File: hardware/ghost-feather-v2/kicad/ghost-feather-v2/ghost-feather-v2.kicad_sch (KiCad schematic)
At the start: 21 parts, among them J1 Conn_ARM_SWD_TagConnect_TC203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, SW1 BOOT0, U1 STM32F722RETx, U2 BMI088

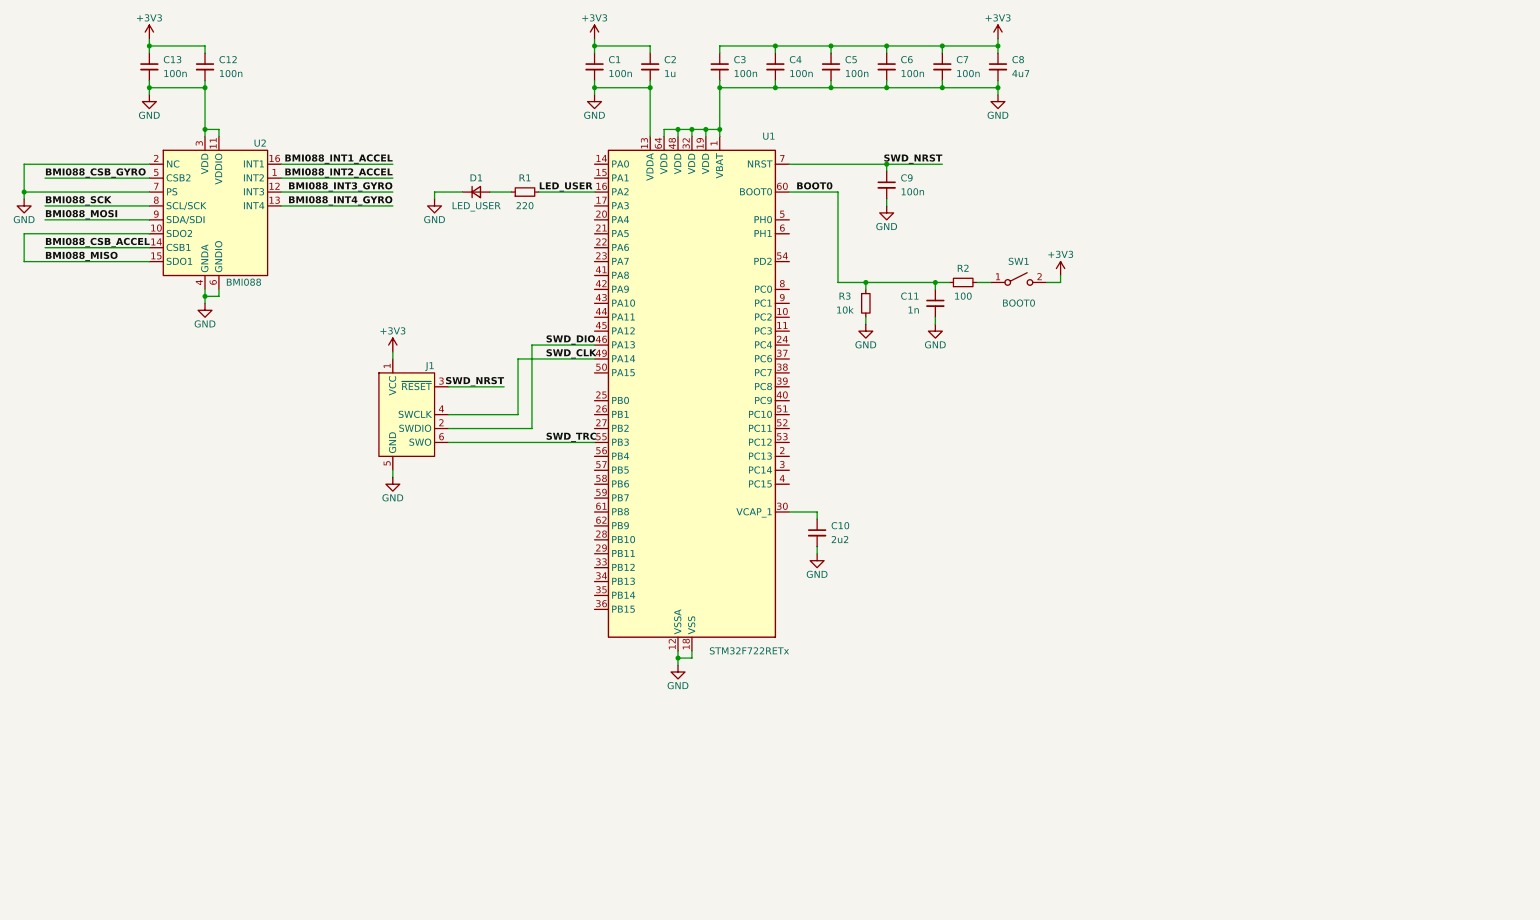
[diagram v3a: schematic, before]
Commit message: feat: hardware: Add ghost-feather-v2 IIS2MDCTR sensor
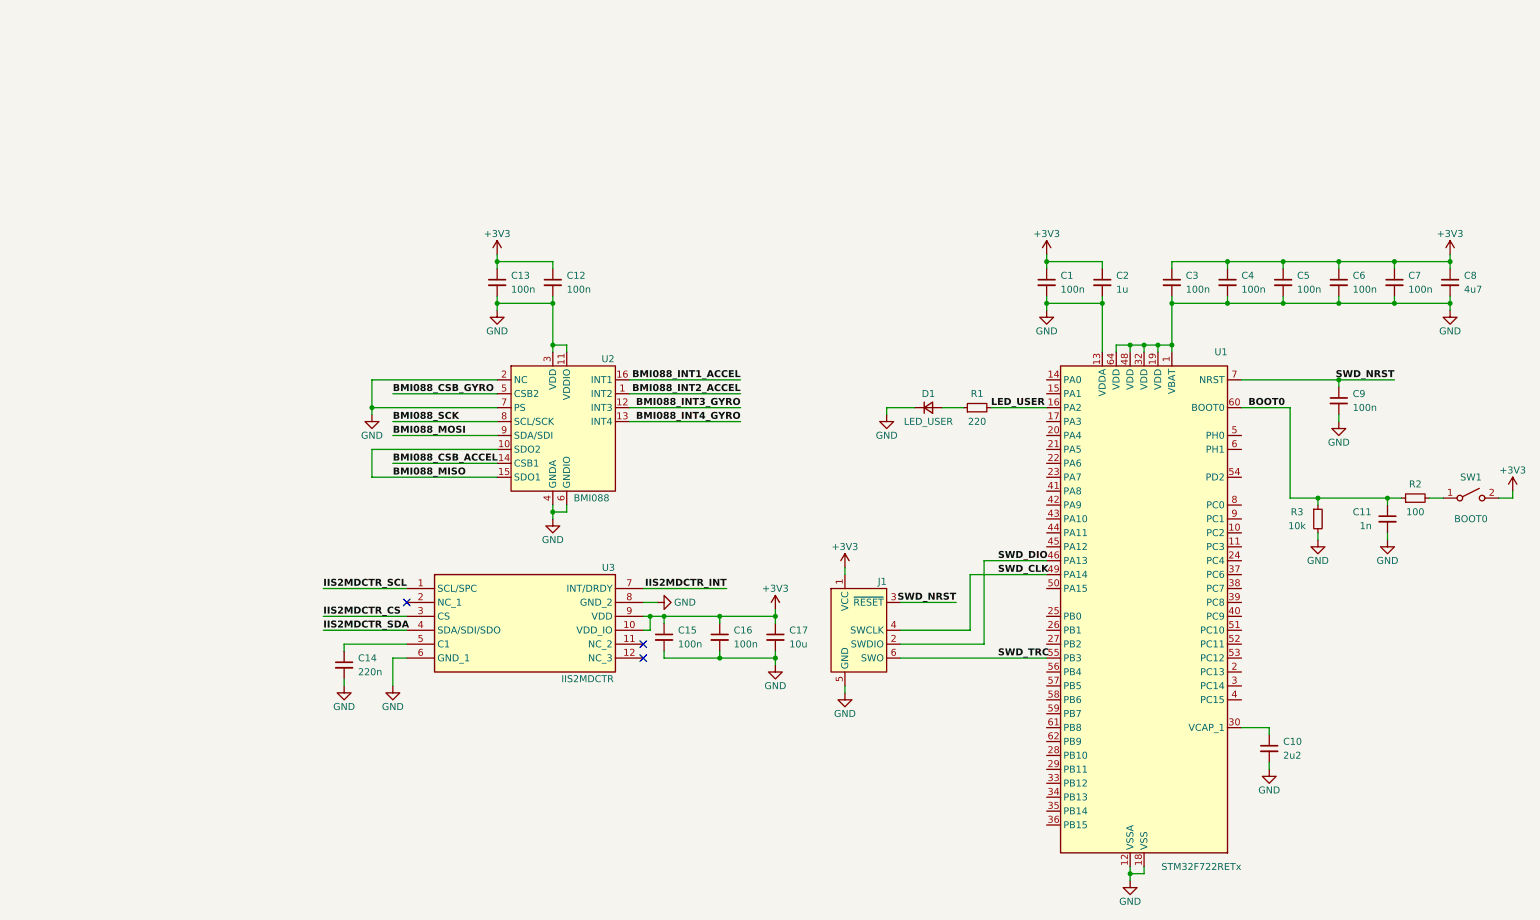
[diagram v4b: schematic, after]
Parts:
- added C14: 220n, symbol Device:C_Small
- added C15, C16: 100n, symbol Device:C_Small
- added C17: 10u, symbol Device:C_Small
- added U3: IIS2MDCTR, IIS2MDCTR, symbol IIS2MDCTR:IIS2MDCTR
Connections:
- net +3V3: now also C15.1, C16.1, C17.1, U3.10 (VDD_IO), U3.9 (VDD)
- net GND: now also C14.2, C15.2, C16.2, C17.2, U3.6 (GND_1), U3.8 (GND_2)
- new net: C14.1, U3.5 (C1)
- new net IIS2MDCTR_CS: U3.3 (CS)
- new net IIS2MDCTR_INT: U3.7 (INT/DRDY)
- new net IIS2MDCTR_SCL: U3.1 (SCL/SPC)
- new net IIS2MDCTR_SDA: U3.4 (SDA/SDI/SDO)
- no-connect marks 0 -> 3
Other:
- moved on the sheet: C1, C10, C11, C12, C13, C2, C3, C4, C5, C6, C7, C8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

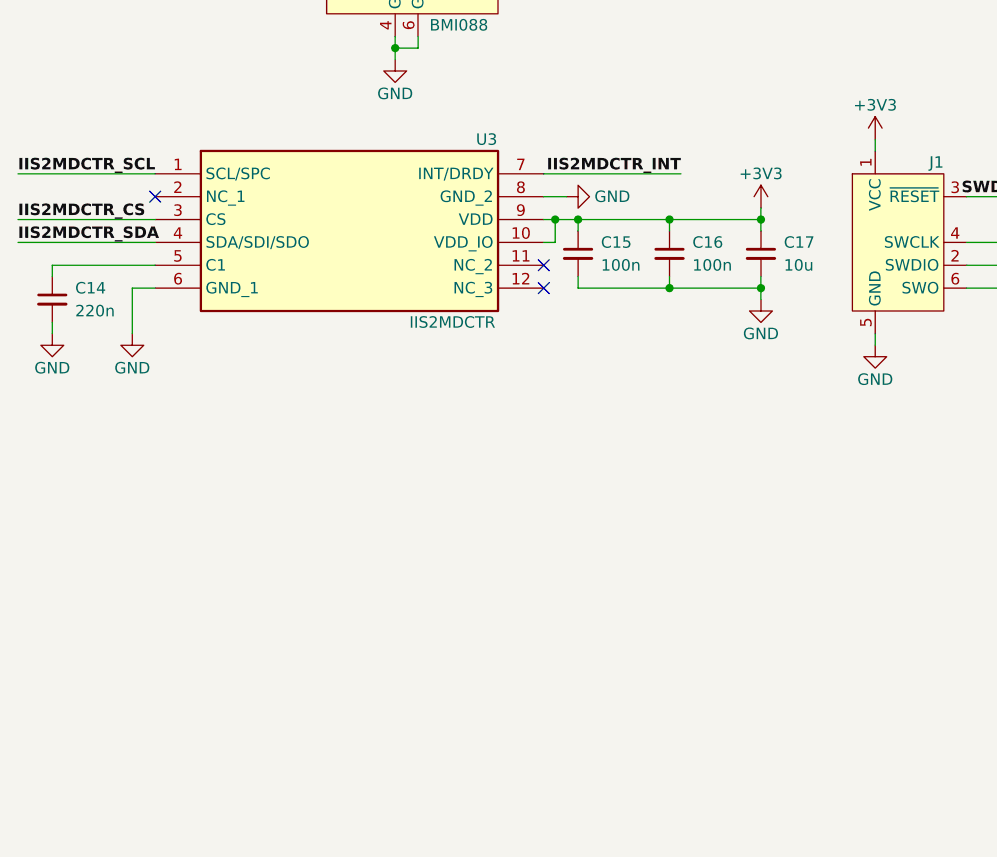
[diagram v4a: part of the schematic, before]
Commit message: feat: hardware: Add ghost-feather-v2 BMP390 sensor
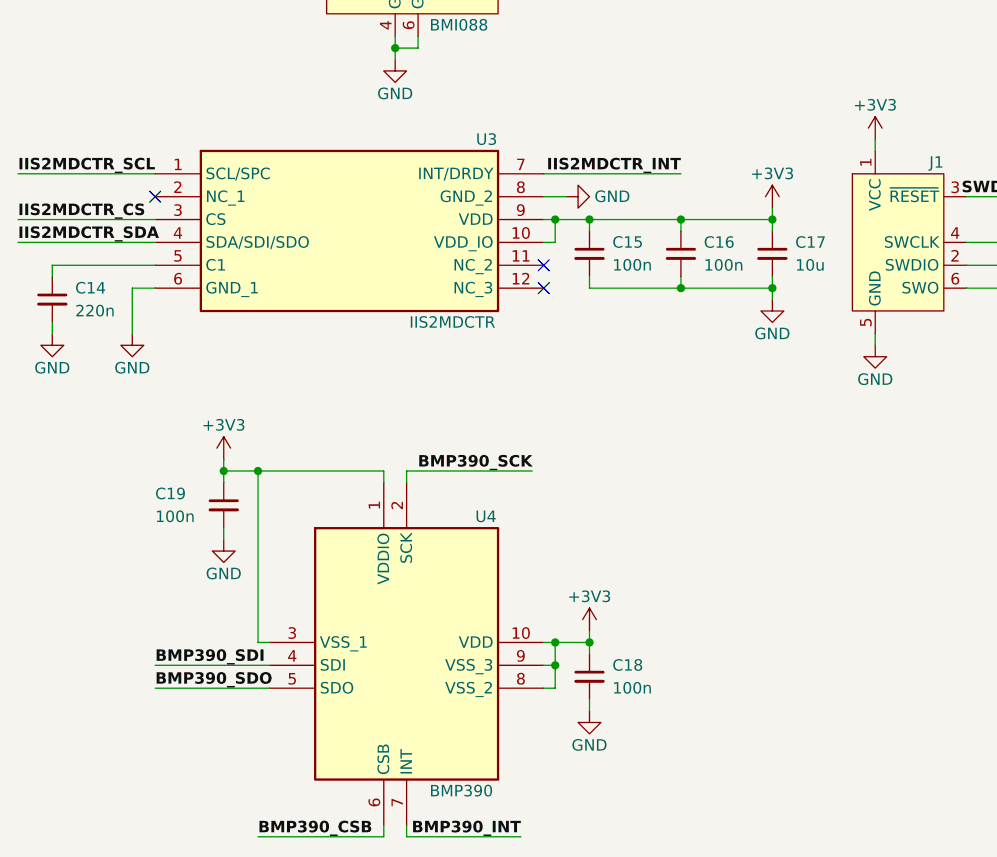
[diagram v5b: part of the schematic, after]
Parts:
- added C18, C19: 100n, symbol Device:C_Small
- added U4: BMP390, BMP390, symbol BMP390:BMP390
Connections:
- net +3V3: now also C18.1, C19.1, U4.1 (VDDIO), U4.10 (VDD), U4.3 (VSS_1), U4.8 (VSS_2), U4.9 (VSS_3)
- net GND: now also C18.2, C19.2
- new net BMP390_CSB: U4.6 (CSB)
- new net BMP390_INT: U4.7 (INT)
- new net BMP390_SCK: U4.2 (SCK)
- new net BMP390_SDI: U4.4 (SDI)
- new net BMP390_SDO: U4.5 (SDO)
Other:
- moved on the sheet: C15, C16, C17

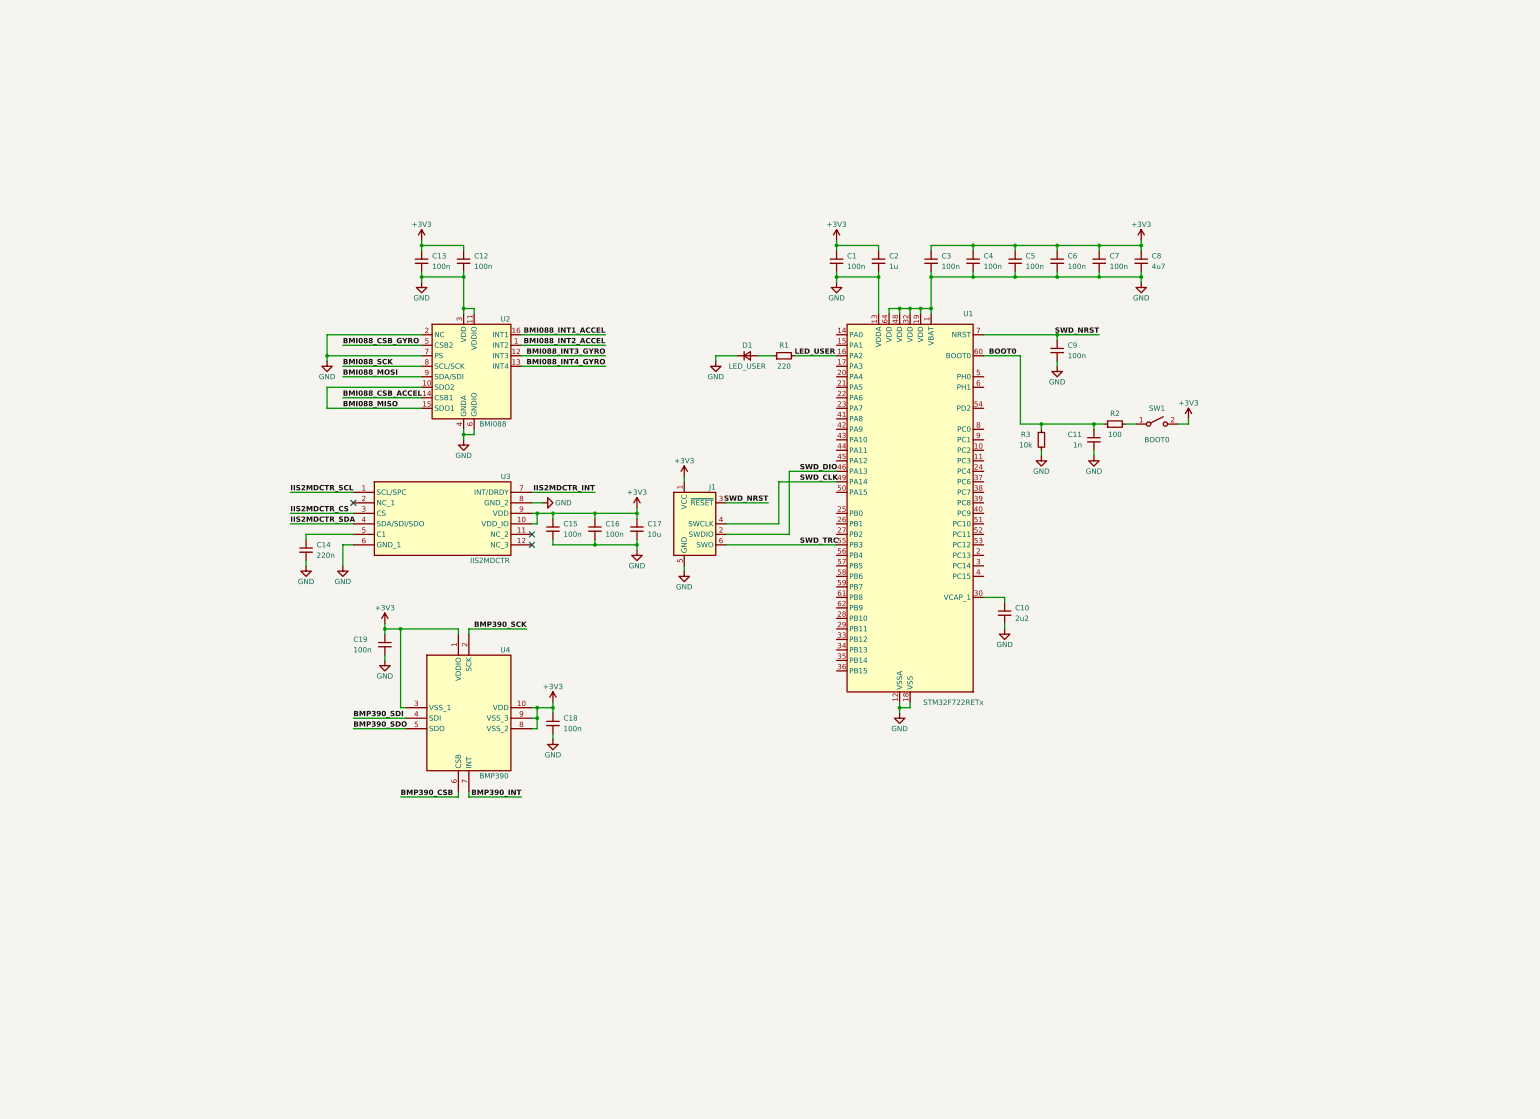
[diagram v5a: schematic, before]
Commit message: feat: hardware: wip: Add USB, SENSORS and MCU sectors on schematic
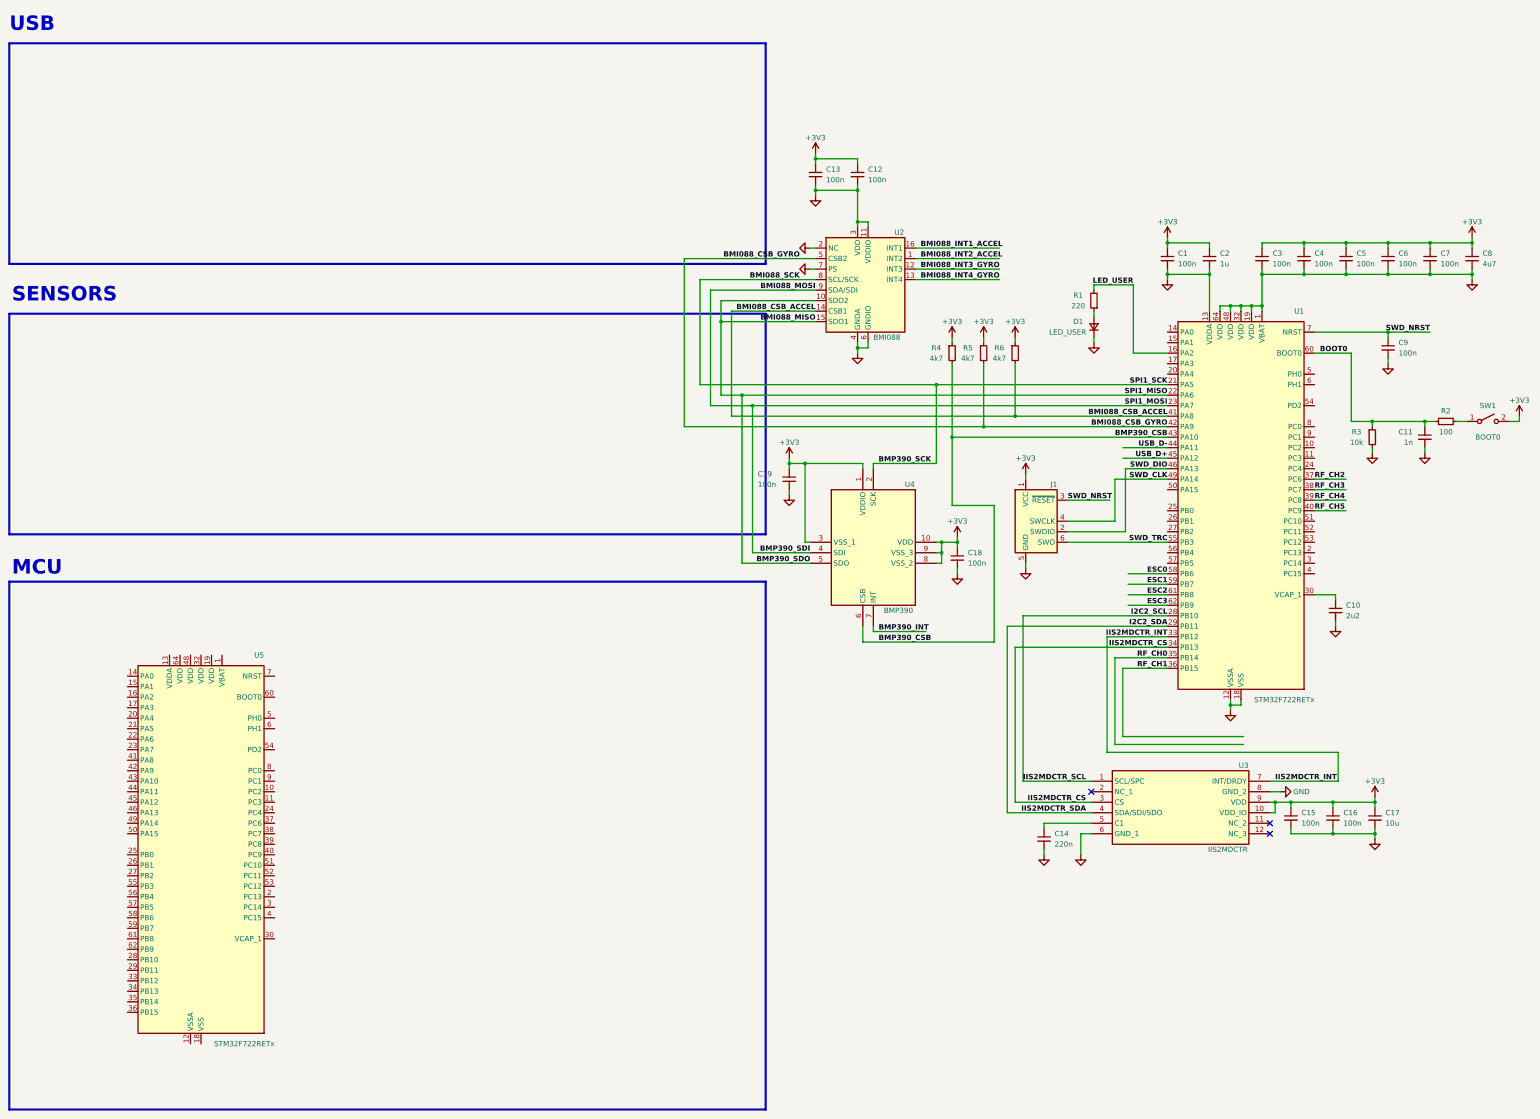
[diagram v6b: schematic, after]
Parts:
- added R4, R5, R6: 4k7, symbol Device:R_Small
- added U5: STM32F722RETx, Package_QFP:LQFP-64_10x10mm_P0.5mm, symbol MCU_ST_STM32F7:STM32F722RETx
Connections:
- net BMP390_SCK is gone; now on net BMI088_SCK: U4.2 (SCK)
- net BMP390_SDI is gone; now on net BMI088_MOSI: U4.4 (SDI)
- net BMP390_SDO is gone; now on net BMI088_MISO: U4.5 (SDO)
- net IIS2MDCTR_SCL is gone; now on net I2C2_SCL: U3.1 (SCL/SPC)
- net IIS2MDCTR_SDA is gone; now on net I2C2_SDA: U3.4 (SDA/SDI/SDO)
- net +3V3: now also R4.1, R5.1, R6.1
- net BMI088_CSB_ACCEL: now also U1.41 (PA8), R6.2
- net BMI088_CSB_GYRO: now also U1.42 (PA9), R5.2
- net BMI088_MISO: now also U1.22 (PA6)
- net BMI088_MOSI: now also U1.23 (PA7)
- net BMI088_SCK: now also U1.21 (PA5)
- net BMP390_CSB: now also U1.43 (PA10), R4.2
- net IIS2MDCTR_CS: now also U1.34 (PB13)
- net IIS2MDCTR_INT: now also U1.33 (PB12)
- net I2C2_SCL: now reaches U1.28 (PB10)
- net I2C2_SDA: now reaches U1.29 (PB11)
- net RF_CH0: now reaches U1.35 (PB14)
- net RF_CH1: now reaches U1.36 (PB15)
- net RF_CH2: now reaches U1.37 (PC6)
- net RF_CH3: now reaches U1.38 (PC7)
- net RF_CH4: now reaches U1.39 (PC8)
- net RF_CH5: now reaches U1.40 (PC9)
- net USB_D-: now reaches U1.44 (PA11)
- net USB_D+: now reaches U1.45 (PA12)
- net ESC0: now reaches U1.58 (PB6)
- net ESC1: now reaches U1.59 (PB7)
- net ESC2: now reaches U1.61 (PB8)
- net ESC3: now reaches U1.62 (PB9)
- new net: U5.18 (VSS), U5.31 (VSS), U5.47 (VSS), U5.63 (VSS)
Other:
- note added: "MCU"
- note added: "SENSORS"
- note added: "USB"
- moved on the sheet: C1, C10, C11, C12, C13, C14, C15, C16, C17, C18, C19, C2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
